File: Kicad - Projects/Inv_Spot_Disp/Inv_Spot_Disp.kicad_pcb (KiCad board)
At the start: 2 copper layers, 128.6 x 75.3 mm, 44 parts, among them J1 PWM_Out, J2 Power_Supply, J3 Current_Sense, J4 Prog, SW1 1, SW2 2, SW3 3, SW4 4, SW5 SW_Push, U1 STM32F030F4Px, U2 NHD-0420H1Z, U3 AMS1117-3.3, U4 LKS561, U5 LM358, U6 LTV-817S

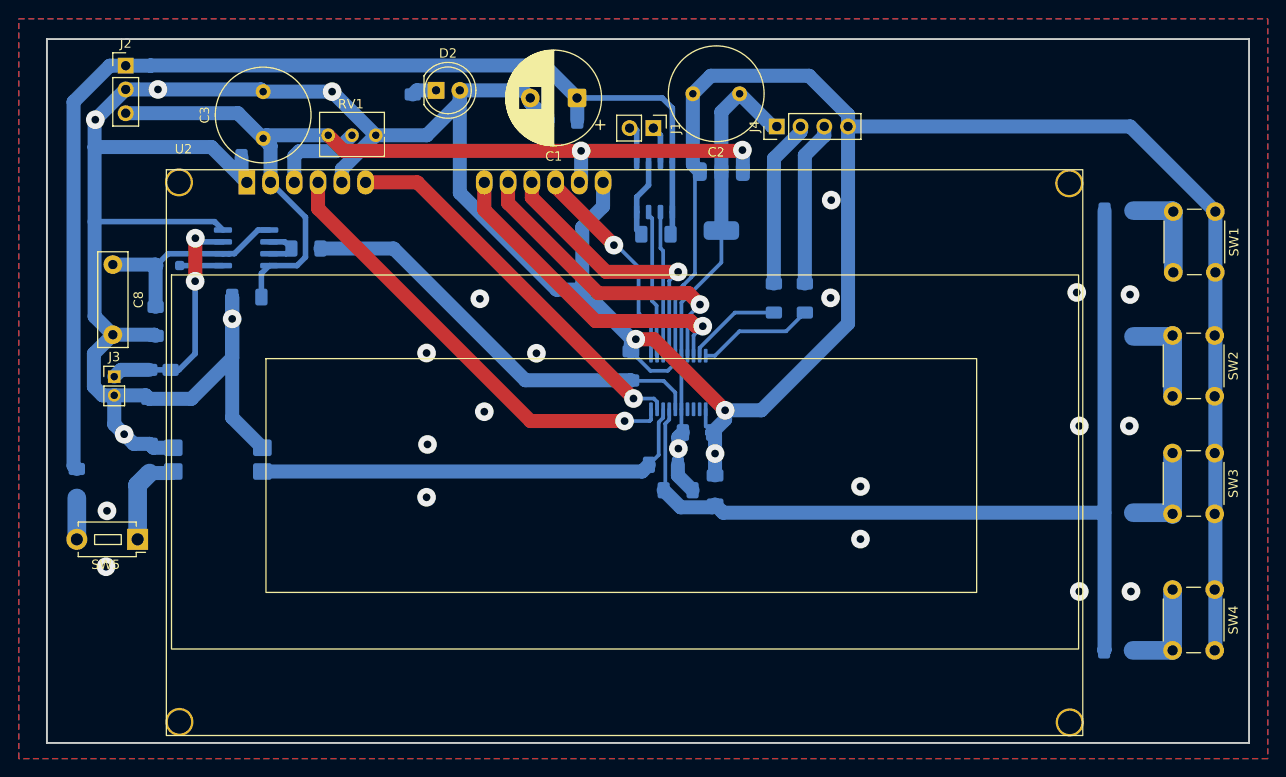
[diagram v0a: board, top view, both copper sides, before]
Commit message: Semi-final Touches
Menu now uses power instead of current

Removed pulsed timing from "CARVAO" and "ARRUELA" operation modes

Added parafix mode

Fixed schematic for output transformer

Added rectification on the output

Trying different power trace geometry in antecipation of voltage spikes
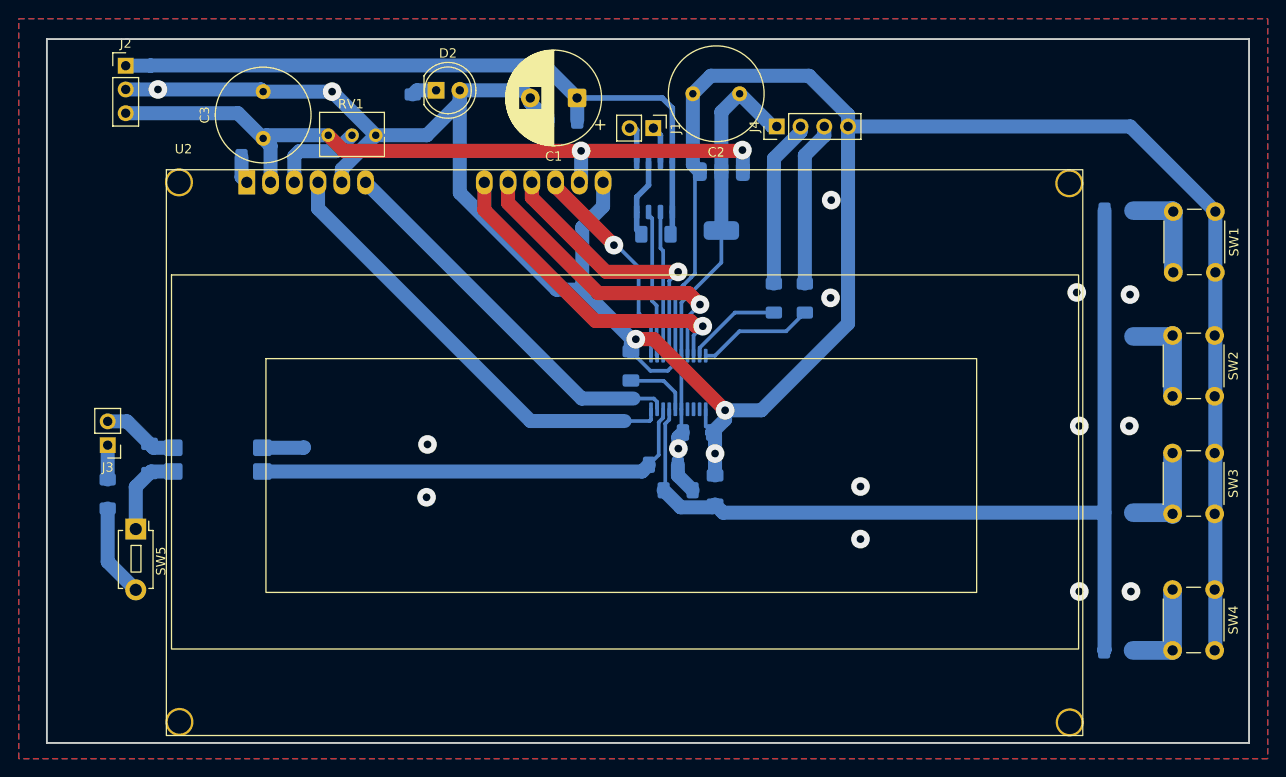
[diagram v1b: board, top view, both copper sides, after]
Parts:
- removed C11: 104, Capacitor_SMD:C_1206_3216Metric_Pad1.33x1.80mm_HandSolder
- removed C8: 104, Capacitor_THT:C_Rect_L10.0mm_W3.0mm_P7.50mm_MKS4
- removed D1: K7, Diode_SMD:D_SOD-323_HandSoldering
- removed R10, R13, R6: 100, Resistor_SMD:R_1206_3216Metric_Pad1.30x1.75mm_HandSolder
- removed R7: 10k, Resistor_SMD:R_1206_3216Metric_Pad1.30x1.75mm_HandSolder
- removed U5: LM358, Package_SO:SOIC-8_3.9x4.9mm_P1.27mm
- J3: value Current_Sense -> Trigger; footprint Connector_PinHeader_2.00mm:PinHeader_1x02_P2.00mm_Vertical -> Connector_PinHeader_2.54mm:PinHeader_1x02_P2.54mm_Vertical
- moved J3 7.36 mm to (35.0, 92.8), turned to 180 degrees
- moved R8 3.49 mm to (35.0, 98.0)
- moved SW5 1.12 mm to (38.0, 101.8), turned to -90 degrees
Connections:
- C9 pad 2: GND -> TGND
- J3 pad 1: Net-(J3-Pin_1) -> 24V
- J3 pad 2: GND -> TGND
- R8 pad 2: 15V -> 24V
- U6 pad 2: GND -> TGND
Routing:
- net GND: track 451.2 -> 332.7 mm, vias 26 -> 17
- net 15V: track 122.9 -> 76.3 mm
- net Current_Sense: track 46.1 -> 7.07 mm
- net Net-(J3-Pin_1): track 25.1 -> 0.00 mm, vias 2 -> 0
- net Net-(D1-K): track 22.8 -> 0.00 mm
- net 5V: track 96.2 -> 78.7 mm
- net TGND: track 0.00 -> 8.18 mm
- net Net-(R8-Pad1): track 4.42 -> 9.94 mm
- net Net-(U5B--): track 5.28 -> 0.00 mm
- net Net-(D1-A): track 4.63 -> 0.00 mm
- net 24V: track 0.00 -> 3.67 mm
- net Net-(C9-Pad1): track 10.2 -> 9.20 mm
- net RS: vias 1 -> 0
- net Enable: vias 1 -> 0

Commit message: Adicionado Regulador 5V - Display
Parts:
- added C7: 10u, Capacitor_THT:C_Radial_D10.0mm_H12.5mm_P5.00mm, F.Cu at (37.3, 66.1)
- added C8: 104, Capacitor_SMD:C_1206_3216Metric_Pad1.33x1.80mm_HandSolder, B.Cu at (35.8, 63.4)
- added U5: L7805, Package_TO_SOT_SMD:TO-252-2, B.Cu at (43.3, 74.3)
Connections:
- J2 pad 3: 5V -> 7V
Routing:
- net 7V: track 0.00 -> 14.0 mm
- net GND: track 332.7 -> 346.7 mm
- net 5V: track 78.7 -> 76.5 mm

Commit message: Updates
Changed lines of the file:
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@@
 			(at -6.7709 -3.56 0)
 			(layer "F.SilkS")
+			(hide yes)
 			(effects
 				(font
@@
 			(at -5.2609 34.91 0)
 			(layer "F.Fab")
+			(hide yes)
 			(effects
 				(font
@@
 		(fp_rect
 			(start -8.0509 9.9)
-			(end 88.9491 49.9)
+			(end 88.7 49.9)
 			(stroke
 				(width 0.1)
@@
 			(layer "F.CrtYd")
 		)
-		(fp_text user "${REFERENCE}"
-			(at 29.4191 14.99 0)
-			(layer "F.Fab")
-			(effects
-				(font
-					(size 1 1)
-					(thickness 0.1)
-				)
-			)
-		)
-		(pad "" thru_hole circle
-			(at -7.25 0)
-			(size 3 3)
-			(drill 2.5)
-			(layers "*.Cu" "*.Mask")
-			(remove_unused_layers no)
-		)
-		(pad "" thru_hole circle
-			(at -7.2009 57.7)
-			(size 3 3)
-			(drill 2.5)
-			(layers "*.Cu" "*.Mask")
-			(remove_unused_layers no)
-		)
-		(pad "" thru_hole circle
-			(at 87.9491 0.1)
-			(size 3 3)
-			(drill 2.5)
-			(layers "*.Cu" "*.Mask")
-			(remove_unused_layers no)
-		)
-		(pad "" thru_hole circle
-			(at 87.9991 57.75)
-			(size 3 3)
-			(drill 2.5)
+		(pad "" thru_hole circle
+			(at -6.15 1.15)
+			(size 4 4)
+			(drill 3)
+			(layers "*.Cu" "*.Mask")
+			(remove_unused_layers no)
+		)
+		(pad "" thru_hole circle
+			(at -6.1 56.65)
+			(size 4 4)
+			(drill 3)
+			(layers "*.Cu" "*.Mask")
+			(remove_unused_layers no)
+		)
+		(pad "" thru_hole circle
+			(at 86.9 1.15 180)
+			(size 4 4)
+			(drill 3)
+			(layers "*.Cu" "*.Mask")
+			(remove_unused_layers no)
+		)
+		(pad "" thru_hole circle
+			(at 86.9 56.65)
+			(size 4 4)
+			(drill 3)
 			(layers "*.Cu" "*.Mask")
 			(remove_unused_layers no)
 		)
 		(pad "1" thru_hole rect
-			(at 0 0)
+			(at 1.4 0)
 			(size 1.8 2.6)
 			(drill 1.2)
@@
 		)
 		(pad "2" thru_hole oval
-			(at 2.54 0)
+			(at 3.94 0)
 			(size 1.8 2.6)
 			(drill 1.2)
@@
 		)
 		(pad "3" thru_hole oval
-			(at 5.08 0)
+			(at 6.48 0)
 			(size 1.8 2.6)
 			(drill 1.2)
@@
 		)
 		(pad "4" thru_hole oval
-			(at 7.62 0)
+			(at 9.02 0)
 			(size 1.8 2.6)
 			(drill 1.2)
@@
 		)
 		(pad "5" thru_hole oval
-			(at 10.16 0)
+			(at 11.56 0)
 			(size 1.8 2.6)
 			(drill 1.2)
@@
 		)
 		(pad "6" thru_hole oval
-			(at 12.7 0)
+			(at 14.1 0)
 			(size 1.8 2.6)
 			(drill 1.2)
@@
 		)
 		(pad "11" thru_hole oval
-			(at 25.4 0)
+			(at 26.8 0)
 			(size 1.8 2.6)
 			(drill 1.2)
@@
 		)
 		(pad "12" thru_hole oval
-			(at 27.94 0)
+			(at 29.34 0)
 			(size 1.8 2.6)
 			(drill 1.2)
@@
 		)
 		(pad "13" thru_hole oval
-			(at 30.48 0)
+			(at 31.88 0)
 			(size 1.8 2.6)
 			(drill 1.2)
@@
 		)
 		(pad "14" thru_hole oval
-			(at 33.02 0)
+			(at 34.42 0)
 			(size 1.8 2.6)
 			(drill 1.2)
@@
 		)
 		(pad "15" thru_hole oval
-			(at 35.56 0)
+			(at 36.96 0)
 			(size 1.8 2.6)
 			(drill 1.2)
@@
 		)
 		(pad "16" thru_hole oval
-			(at 38.1 0)
-			(size 1.8 2.6)
-			(drill 1.2)
+			(at 39.5 0)
+			(size 1.8 2.6)
+			(drill 1.2)
